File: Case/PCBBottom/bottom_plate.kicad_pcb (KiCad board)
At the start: 2 copper layers, 143.5 x 115.5 mm, 5 parts

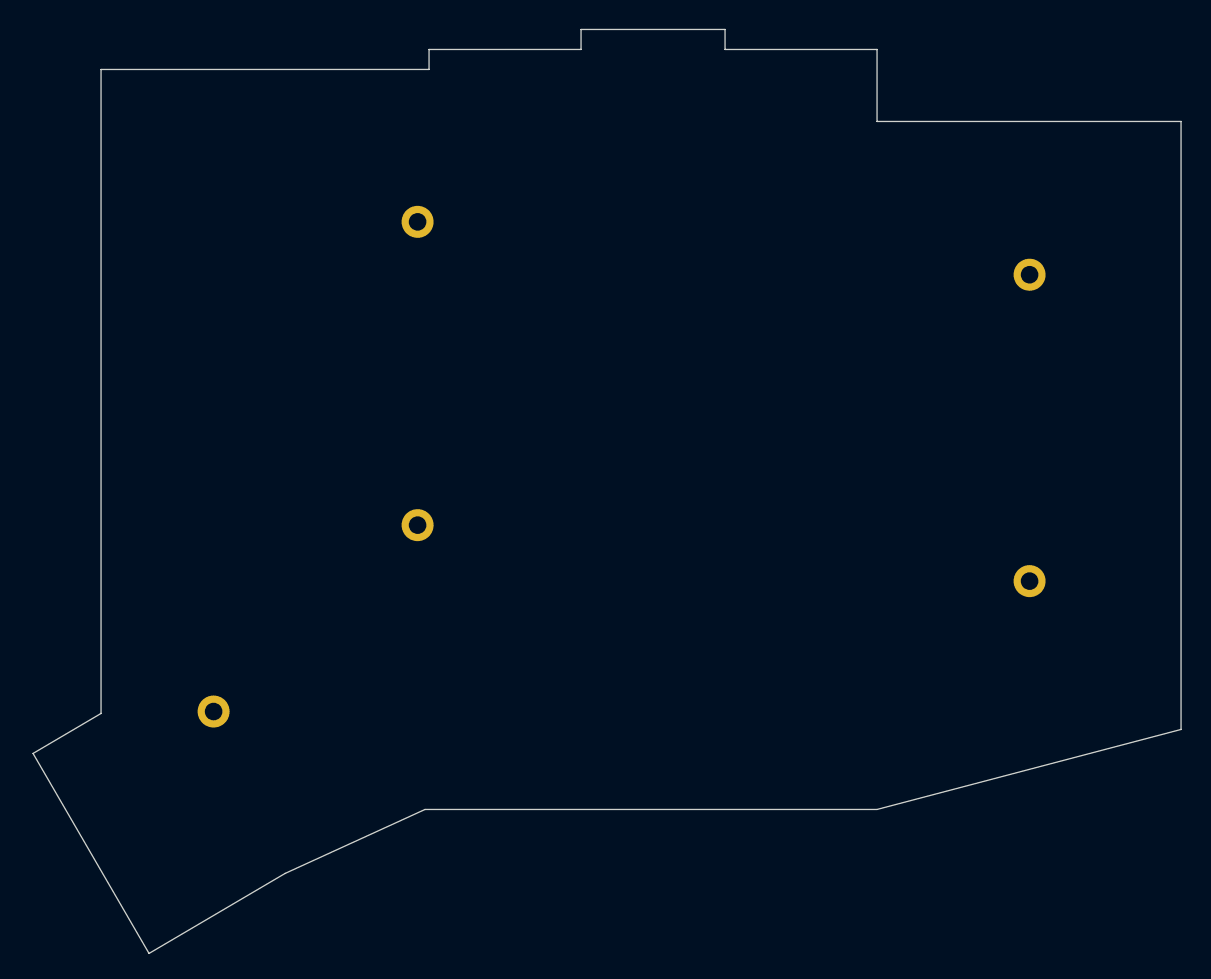
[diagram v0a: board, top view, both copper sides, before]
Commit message: Add logos and credits on all boards
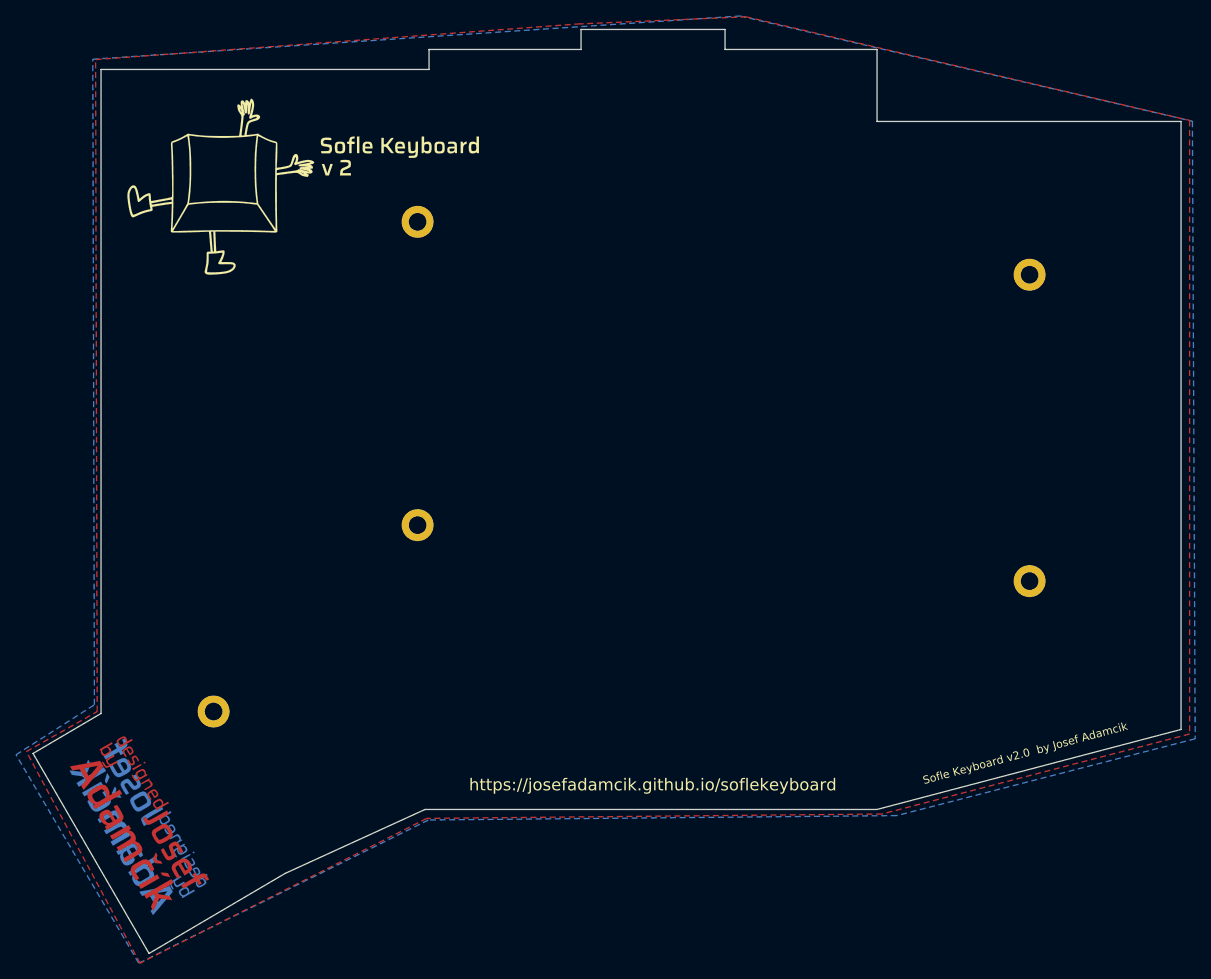
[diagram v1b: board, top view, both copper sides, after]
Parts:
- added Ref**: Val**, SofleKeyboard-footprint:josef_adamcik_20mm_cu_mask, B.Cu at (51.5, 147.1)
- added Ref**: Val**, SofleKeyboard-footprint:josef_adamcik_20mm_cu_mask, F.Cu at (51.2, 145.9)
- added Ref**: Val**, SofleKeyboard-footprint:SofleV2Logo2, F.Cu at (63.2, 68.6)
- added Ref**: Val**, SofleKeyboard-footprint:SofleV2Logo, B.Cu at (67.5, 68.8)
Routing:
- added copper zone on B.Cu, net (none)
- added copper zone on F.Cu, net (none)
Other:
- board text added: "Sofle Keyboard v2.0 by Josef Adamcik"
- board text added: "https://josefadamcik.github.io/soflekeyboard"

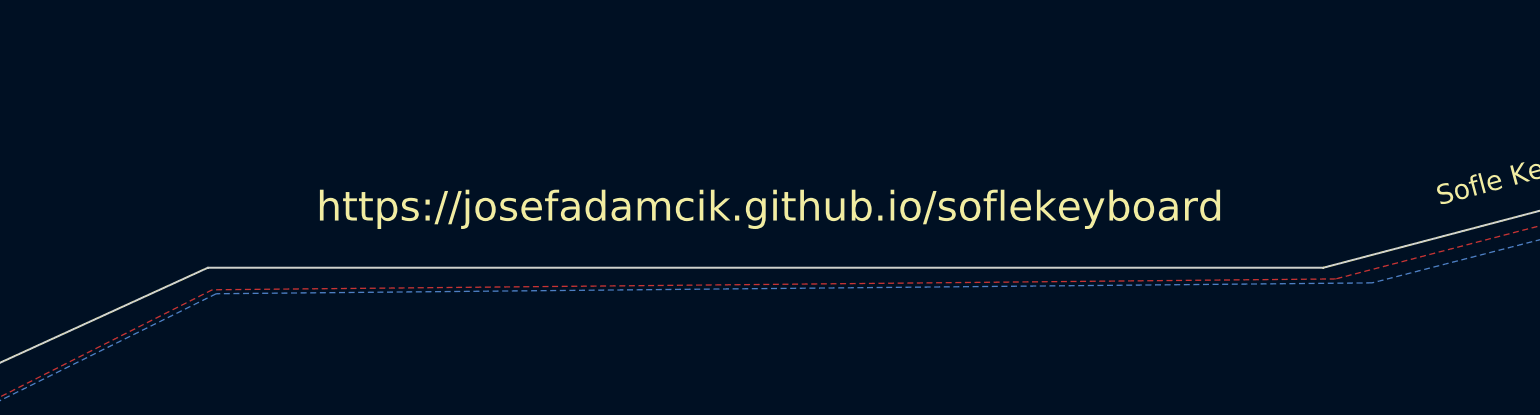
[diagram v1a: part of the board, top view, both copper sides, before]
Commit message: Small improvements to plates
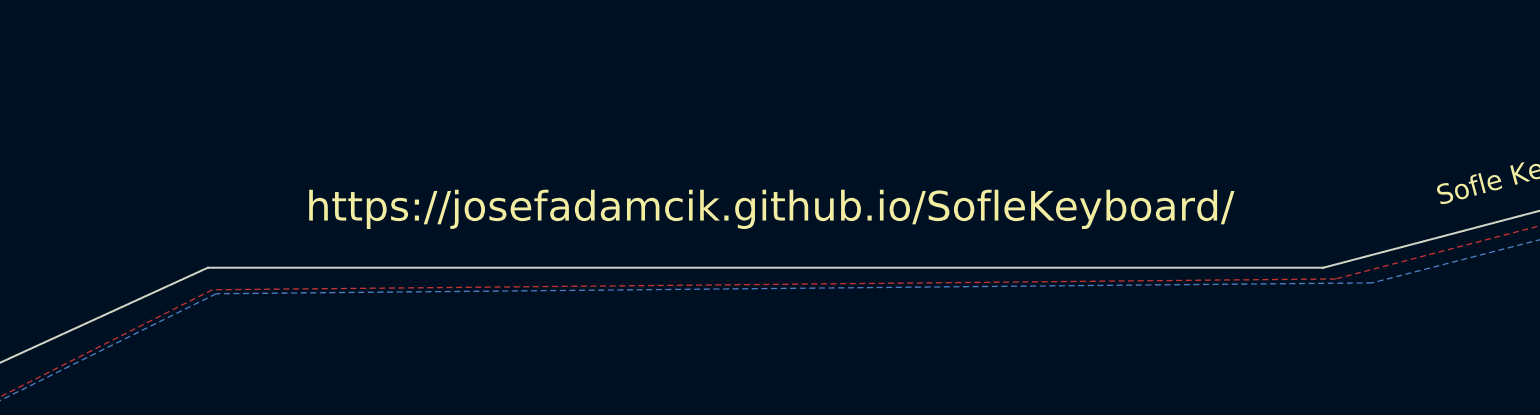
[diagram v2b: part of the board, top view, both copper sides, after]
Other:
- board text added: "https://josefadamcik.github.io/SofleKeyboard/"
- board text removed: "https://josefadamcik.github.io/soflekeyboard"
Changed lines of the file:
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@@
   (page A4)
   (layers
-    (0 F.Cu signal)
+    (0 F.Cu signal hide)
     (31 B.Cu signal)
-    (32 B.Adhes user)
-    (33 F.Adhes user)
+    (32 B.Adhes user hide)
+    (33 F.Adhes user hide)
     (34 B.Paste user)
-    (35 F.Paste user)
+    (35 F.Paste user hide)
     (36 B.SilkS user)
-    (37 F.SilkS user)
+    (37 F.SilkS user hide)
     (38 B.Mask user)
-    (39 F.Mask user)
-    (40 Dwgs.User user)
-    (41 Cmts.User user)
-    (42 Eco1.User user)
-    (43 Eco2.User user)
+    (39 F.Mask user hide)
+    (40 Dwgs.User user hide)
+    (41 Cmts.User user hide)
+    (42 Eco1.User user hide)
+    (43 Eco2.User user hide)
     (44 Edge.Cuts user)
-    (45 Margin user)
+    (45 Margin user hide)
     (46 B.CrtYd user)
-    (47 F.CrtYd user)
+    (47 F.CrtYd user hide)
     (48 B.Fab user)
-    (49 F.Fab user)
+    (49 F.Fab user hide)
   )
   (setup
@@
     (pad 5 thru_hole circle (at 0 0) (size 4 4) (drill 2.2) (layers *.Cu *.Mask))
   )
-  (gr_text https://josefadamcik.github.io/soflekeyboard (at 118.65 139.6) (layer B.SilkS)
+  (gr_text https://josefadamcik.github.io/SofleKeyboard/ (at 118.65 139.6) (layer B.SilkS)
     (effects (font (size 1.5 1.5) (thickness 0.3)) (justify mirror))
   )
-  (gr_text https://josefadamcik.github.io/soflekeyboard (at 118.8 139.6) (layer F.SilkS)
+  (gr_text https://josefadamcik.github.io/SofleKeyboard/ (at 118.8 139.6) (layer F.SilkS)
     (effects (font (size 1.5 1.5) (thickness 0.3)))
   )
